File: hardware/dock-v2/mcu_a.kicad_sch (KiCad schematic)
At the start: 29 parts, among them SW301 SW_Push, SW302 SW_Push, U301 RP2354A, Y301 12MHz

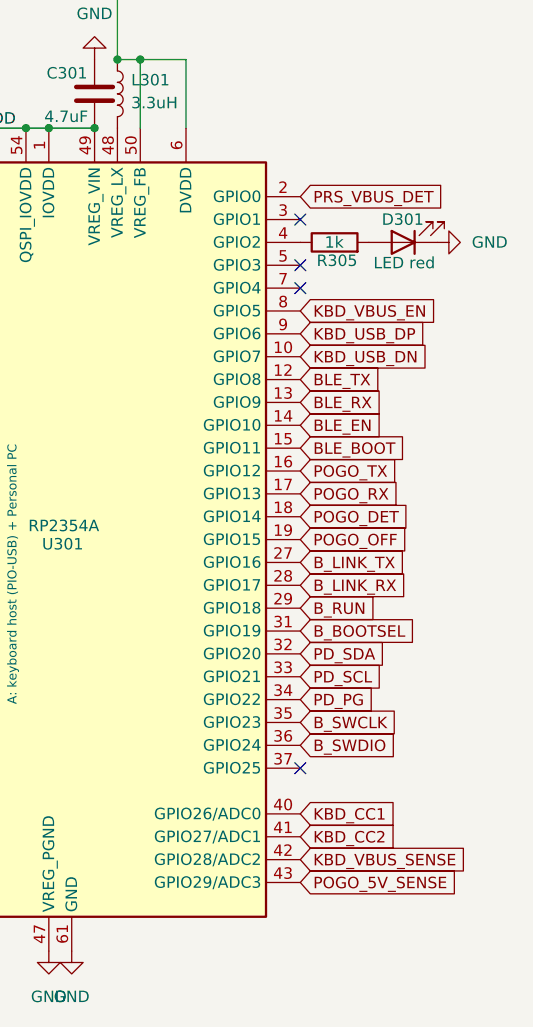
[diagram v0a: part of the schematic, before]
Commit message: Dock v2: MCU A/B GPIO map reassigned for routing (ESP32 front-left, 2-layer goal)
A: KBD PIO-USB on GPIO2/3 (DMDP), BLE on UART0 GPIO12/13, pogo on the
bottom pins, CH224A on I2C1 GPIO18/19 (+PG 17) routed under B, B
RUN/SWD on GPIO20-22, B link on UART1 GPIO23/24, BOOTSEL B on GPIO25,
ADC order reversed. B: link on GPIO5/6, WRK_VBUS_DET on GPIO29.
Docs: GPIO numbers in DOCK_CONNECTIONS now come from dock_nets.py.

Co-Authored-By: Claude Opus 5.5 <noreply@anthropic.com>
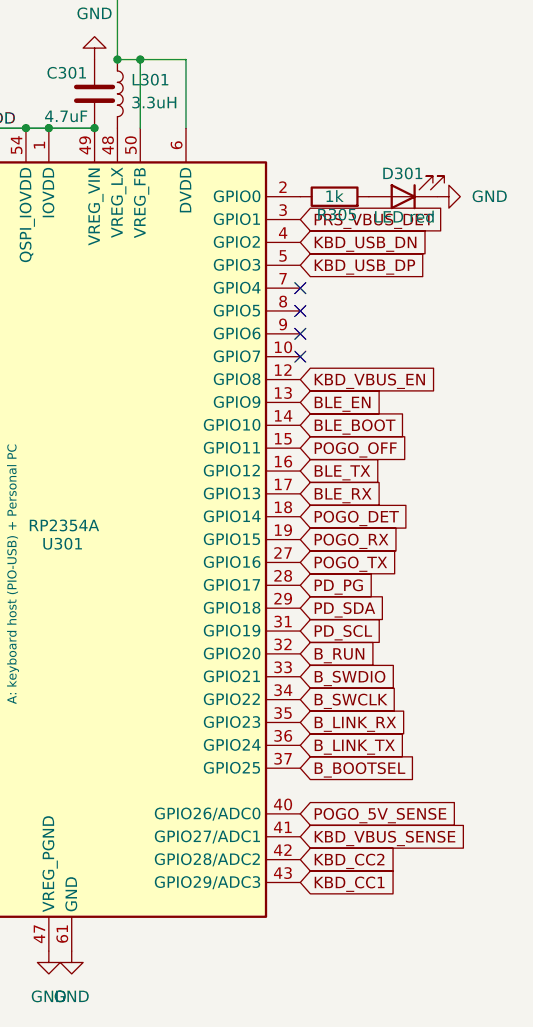
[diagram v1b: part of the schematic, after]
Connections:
- net BLE_BOOT: now also U301.14 (GPIO10); no longer U301.15 (GPIO11)
- net BLE_EN: now also U301.13 (GPIO9); no longer U301.14 (GPIO10)
- net BLE_RX: now also U301.17 (GPIO13); no longer U301.13 (GPIO9)
- net BLE_TX: now also U301.16 (GPIO12); no longer U301.12 (GPIO8)
- net B_BOOTSEL: now also U301.37 (GPIO25); no longer U301.31 (GPIO19)
- net B_LINK_RX: now also U301.35 (GPIO23); no longer U301.28 (GPIO17)
- net B_LINK_TX: now also U301.36 (GPIO24); no longer U301.27 (GPIO16)
- net B_RUN: now also U301.32 (GPIO20); no longer U301.29 (GPIO18)
- net B_SWCLK: now also U301.34 (GPIO22); no longer U301.35 (GPIO23)
- net B_SWDIO: now also U301.33 (GPIO21); no longer U301.36 (GPIO24)
- net KBD_CC1: now also U301.43 (GPIO29/ADC3); no longer U301.40 (GPIO26/ADC0)
- net KBD_CC2: now also U301.42 (GPIO28/ADC2); no longer U301.41 (GPIO27/ADC1)
- net KBD_USB_DN: now also U301.4 (GPIO2); no longer U301.10 (GPIO7)
- net KBD_USB_DP: now also U301.5 (GPIO3); no longer U301.9 (GPIO6)
- net KBD_VBUS_EN: now also U301.12 (GPIO8); no longer U301.8 (GPIO5)
- net KBD_VBUS_SENSE: now also U301.41 (GPIO27/ADC1); no longer U301.42 (GPIO28/ADC2)
- net PD_PG: now also U301.28 (GPIO17); no longer U301.34 (GPIO22)
- net PD_SCL: now also U301.31 (GPIO19); no longer U301.33 (GPIO21)
- net PD_SDA: now also U301.29 (GPIO18); no longer U301.32 (GPIO20)
- net POGO_5V_SENSE: now also U301.40 (GPIO26/ADC0); no longer U301.43 (GPIO29/ADC3)
- net POGO_OFF: now also U301.15 (GPIO11); no longer U301.19 (GPIO15)
- net POGO_RX: now also U301.19 (GPIO15); no longer U301.17 (GPIO13)
- net POGO_TX: now also U301.27 (GPIO16); no longer U301.16 (GPIO12)
- net PRS_VBUS_DET: now also U301.3 (GPIO1); no longer U301.2 (GPIO0)
- net at R305.1: now also U301.2 (GPIO0); no longer U301.4 (GPIO2)
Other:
- moved on the sheet: D301, R305

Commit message: Dock v2: routing complete, SWD test pads removed (user's work, snapshot)
Co-Authored-By: Claude Opus 5.5 <noreply@anthropic.com>
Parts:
- removed TP301, TP302, TP303: TestPoint, TestPoint:TestPoint_Pad_D1.0mm, symbol Connector:TestPoint
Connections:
- no-connect marks 9 -> 11

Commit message: Dock v2 PCB: fix unconnected nets, widen power traces, readable silkscreen, 2 copper layers
- MCU A and B IOVDD (pins 30/38) had no 3V3 feed: added an under-chip jumper (A)
  and a top-layer feed to the 3V3 via by the buck (B)
- MCU B's exposed pad sat in a GND pour island: 3V3 bottom ring via moved so the
  plane reaches it; crystal B GND vias added; pour clearance 0.5 -> 0.3 mm
- power traces widened where clearance allows (switch node 1.5 mm, 5 V 1.0 mm,
  VBUS_IN/POGO_5V/KBD_VBUS as far as fits); VBUS_IN vias 0.8/0.4
- silkscreen: refs 0.8/1.0 mm, re-placed clear of pads and parts, labels for
  connectors, buttons, LEDs and ESP32 UART pads; 22 small passives hidden
- copper layers 4 -> 2 (inner layers were empty)
- model/docs: SWD test pads TP301-303/TP401-403 removed

DRC: 0 violations, 0 unconnected, 0 parity issues.

Co-Authored-By: Claude Opus 5.5 <noreply@anthropic.com>
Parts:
- added J401: Conn_01x03, Connector_PinHeader_2.54mm:PinHeader_1x03_P2.54mm_Vertical, symbol Connector_Generic:Conn_01x03
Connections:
- net GND: now also J401.1 (Pin_1)
- net at U301.22 (XOUT): now also R302.1; no longer R302.2
- net at U301.24 (SWCLK): now also J401.3 (Pin_3)
- net at U301.25 (SWDIO): now also J401.2 (Pin_2)
- net at C316.2, Y301.3: now also R302.2; no longer R302.1
- no-connect marks 11 -> 9
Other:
- moved on the sheet: R302
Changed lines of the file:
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@@
 	)
 	(no_connect
-		(at 158.75 154.94)
-	)
-	(no_connect
 		(at 158.75 119.38)
 	)
 	(no_connect
-		(at 158.75 152.4)
-	)
-	(no_connect
 		(at 209.55 99.06)
 	)
@@
 	(wire
 		(pts
+			(xy 148.59 154.94) (xy 158.75 154.94)
+		)
+		(stroke
+			(width 0)
+			(type default)
+		)
+	)
+	(wire
+		(pts
 			(xy 144.78 127) (xy 144.78 129.54)
 		)
@@
 	(wire
 		(pts
+			(xy 148.59 152.4) (xy 158.75 152.4)
+		)
+		(stroke
+			(width 0)
+			(type default)
+		)
+	)
+	(wire
+		(pts
 			(xy 170.18 31.75) (xy 162.56 31.75)
 		)
@@
 	(symbol
 		(lib_id "Device:R")
-		(at 144.78 142.24 90)
+		(at 144.78 142.24 270)
 		(unit 1)
 		(body_style 1)
@@
 		(dnp no)
 		(property "Reference" "R302"
-			(at 146.812 140.208 90)
+			(at 142.748 144.272 90)
 			(show_name no)
 			(do_not_autoplace no)
@@
 		)
 		(property "Value" "1k"
-			(at 146.304 142.24 90)
+			(at 143.256 142.24 90)
 			(show_name no)
 			(do_not_autoplace no)
@@
 		)
 		(property "Note" "XOUT series (RPi R2)"
-			(at 148.59 138.68 0)
+			(at 140.97 145.8 0)
 			(hide yes)
 			(show_name no)
@@
 	)
 	(symbol
+		(lib_id "power:GND")
+		(at 148.59 157.48 90)
+		(unit 1)
+		(body_style 1)
+		(exclude_from_sim no)
+		(in_bom yes)
+		(on_board yes)
+		(in_pos_files yes)
+		(dnp no)
+		(fields_autoplaced yes)
+		(property "Reference" "#PWR0410"
+			(at 154.94 157.48 0)
+			(hide yes)
+			(show_name no)
+			(do_not_autoplace no)
+			(effects
+				(font
+					(size 1.27 1.27)
+				)
+			)
+		)
+		(property "Value" "GND"
+			(at 152.4 157.4799 90)
+			(show_name no)
+			(do_not_autoplace no)
+			(effects
+				(font
+					(size 1.27 1.27)
+				)
+				(justify right)
+			)
+		)
+		(property "Footprint" ""
+			(at 148.59 157.48 0)
+			(hide yes)
+			(show_name no)
+			(do_not_autoplace no)
+			(effects
+				(font
+					(size 1.27 1.27)
+				)
+			)
+		)
+		(property "Datasheet" ""
+			(at 148.59 157.48 0)
+			(hide yes)
+			(show_name no)
+			(do_not_autoplace no)
+			(effects
+				(font
+					(size 1.27 1.27)
+				)
+			)
+		)
+		(property "Description" "Power symbol creates a global label with name \"GND\" , ground"
+			(at 148.59 157.48 0)
+			(hide yes)
+			(show_name no)
+			(do_not_autoplace no)
+			(effects
+				(font
+					(size 1.27 1.27)
+				)
+			)
+		)
+		(pin "1"
+		)
+		(instances
+			(project "dock-v2"
+				(path "/928a9dc6-b0ce-4f47-a17d-f26fd77e396a/bcfba91e-3181-4d07-9970-4b16b455c32a"
+					(reference "#PWR0410")
+					(unit 1)
+				)
+			)
+		)
+	)
+	(symbol
 		(lib_id "power:PWR_FLAG")
 		(at 198.12 38.1 0)
@@
 					(unit 1)
 				)
+			)
+		)
+	)
+	(symbol
+		(lib_id "Connector_Generic:Conn_01x03")
+		(at 143.51 154.94 180)
+		(unit 1)
+		(body_style 1)
+		(exclude_from_sim no)
+		(in_bom yes)
+		(on_board yes)
+		(in_pos_files yes)
+		(dnp no)
+		(property "Reference" "J401"
+			(at 144.526 150.114 0)
+			(show_name no)
+			(do_not_autoplace no)
+			(effects
+				(font
+					(size 1.27 1.27)
+				)
+			)
+		)
+		(property "Value" "Conn_01x03"
+			(at 141.224 154.94 90)
+			(show_name no)
+			(do_not_autoplace no)
+			(effects
+				(font
+					(size 1.27 1.27)
+				)
+			)
+		)
+		(property "Footprint" "Connector_PinHeader_2.54mm:PinHeader_1x03_P2.54mm_Vertical"
+			(at 143.51 154.94 0)
+			(hide yes)
+			(show_name no)
+			(do_not_autoplace no)
+			(effects
+				(font
+					(size 1.27 1.27)
+				)
+			)
+		)
+		(property "Datasheet" ""
+			(at 143.51 154.94 0)
+			(hide yes)
+			(show_name no)
+			(do_not_autoplace no)
+			(effects
+				(font
+					(size 1.27 1.27)
+				)
+			)
+		)
+		(property "Description" "Generic connector, single row, 01x03, script generated (kicad-library-utils/schlib/autogen/connector/)"
+			(at 143.51 154.94 0)
+			(hide yes)
+			(show_name no)
+			(do_not_autoplace no)
+			(effects
+				(font
+					(size 1.27 1.27)
+				)
+			)
+		)
+		(pin "3"
+		)
+		(pin "1"
+		)
+		(pin "2"
+		)
+		(instances
+			(project "dock-v2"
+				(path "/928a9dc6-b0ce-4f47-a17d-f26fd77e396a/bcfba91e-3181-4d07-9970-4b16b455c32a"
+					(reference "J401")
+					(unit 1)
+				)
